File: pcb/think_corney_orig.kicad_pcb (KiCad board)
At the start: 2 copper layers, 128.7 x 86.7 mm, 51 parts

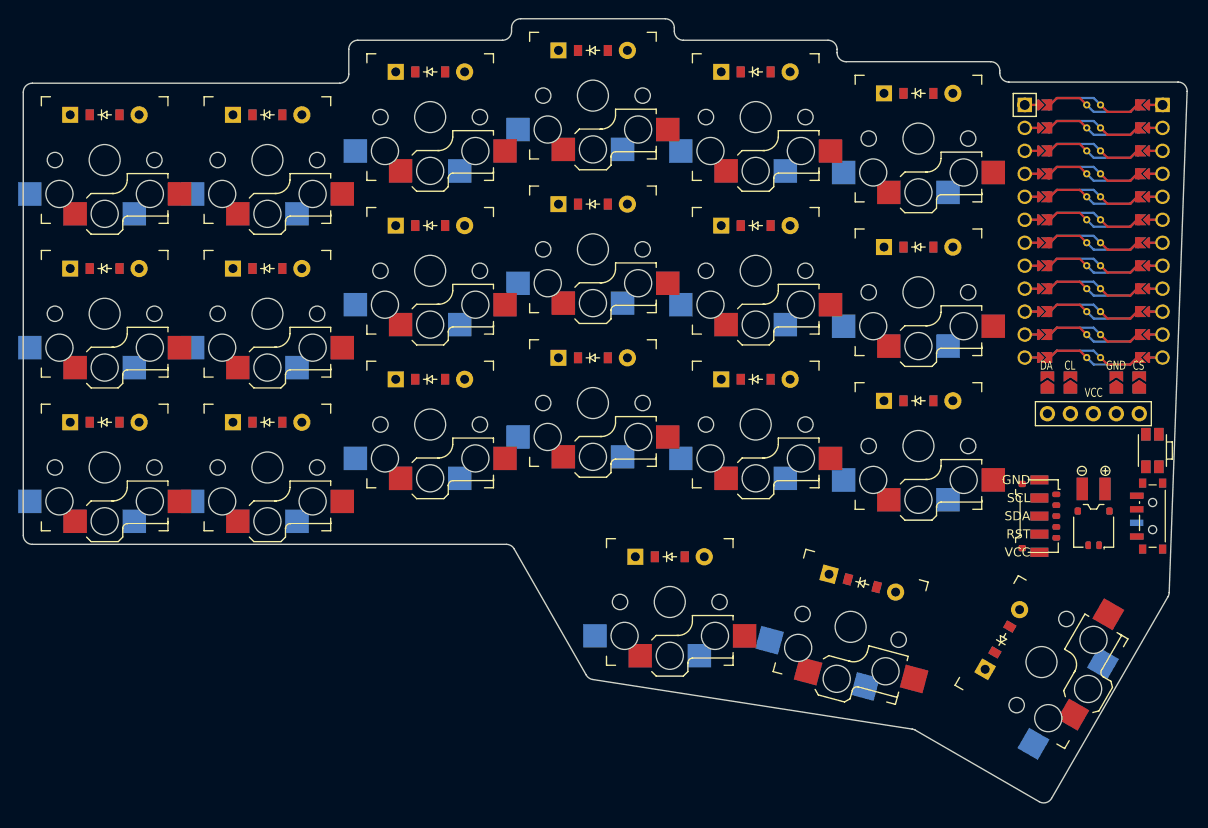
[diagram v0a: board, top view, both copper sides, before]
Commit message: PCB: Add generated pcb version
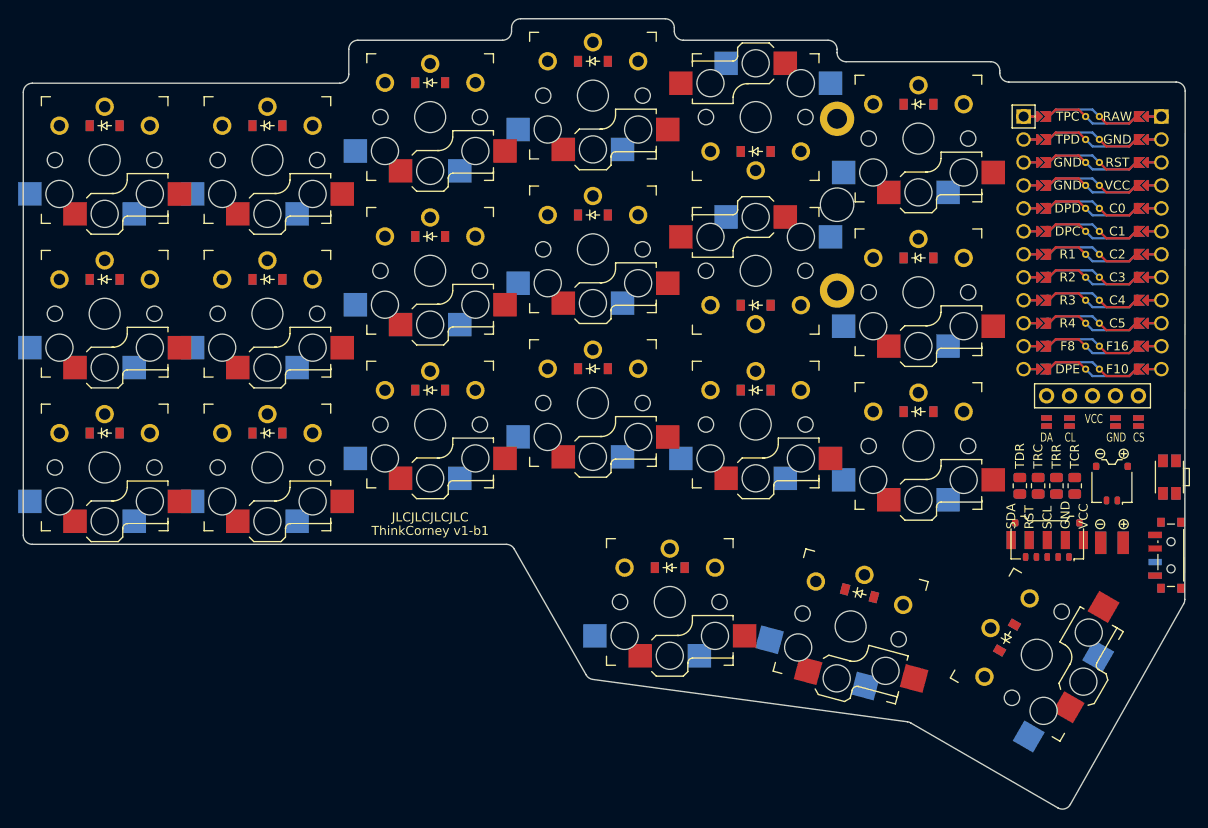
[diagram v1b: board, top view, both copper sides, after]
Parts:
- added ?: , text, F.Cu at (136.0, 107.0)
- added ?: , text, F.Cu at (136.0, 105.5)
- added ICON2: , icon_bat, F.Cu at (211.4, 106.3)
- added SMD1: , smd_805, F.Cu at (204.2, 102.0)
- added TP1: , trackpoint_mount_t430, F.Cu at (181.0, 70.9)
- moved S21 68.1 mm to (172.0, 61.2), turned to 0 degrees
- moved D21 60.5 mm to (172.0, 65.0), turned to 0 degrees
- moved D18 55.7 mm to (183.5, 113.9), turned to -15 degrees
- moved S18 54.5 mm to (182.5, 117.6), turned to -195 degrees
- moved D17 44.9 mm to (162.5, 111.1)
- moved S17 43.9 mm to (162.5, 114.9)
- moved S19 41.0 mm to (203.1, 120.7), turned to -120 degrees
- moved S20 40.8 mm to (172.0, 78.2), turned to 0 degrees
- moved D19 38.4 mm to (199.8, 118.8), turned to 60 degrees
- moved S16 34.0 mm to (190.0, 63.6)
- moved D20 32.9 mm to (172.0, 82.0), turned to 0 degrees
- moved D16 32.8 mm to (190.0, 59.8)
- moved D14 27.3 mm to (190.0, 93.8)
- moved D15 27.3 mm to (190.0, 76.8)
- moved S14 26.4 mm to (190.0, 97.6)
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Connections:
- net P10 renamed F10
- net P16 renamed F16
- net P19 renamed C2
- net P20 renamed C1
- net P21 renamed C0
- net P8 renamed F8
- net TP_RST renamed TPR
- CONN2 pad 1: TP_GND -> VCC
- CONN2 pad 2: TP_SCL -> GND
- CONN2 pad 3: TP_SDA -> TPC
- CONN2 pad 5: TP_VCC -> TPD
- D1 pad 1: P6 -> R3
- D10 pad 1: P6 -> R3
- D11 pad 1: P5 -> R2
- D12 pad 1: P4 -> R1
- D13 pad 1: P6 -> R3
- D14 pad 1: P5 -> R3
- D14 pad 2: index_home -> inner_bottom
- D15 pad 1: P4 -> R2
- D15 pad 2: index_top -> inner_home
- D16 pad 1: P6 -> R1
- D16 pad 2: inner_bottom -> inner_top
- D17 pad 1: P5 -> R4
- D17 pad 2: inner_home -> outer_cluster
- D18 pad 1: P4 -> R4
- D18 pad 2: inner_top -> home_cluster
- D19 pad 1: P7 -> R4
- D19 pad 2: outer_cluster -> inner_cluster
- D2 pad 1: P5 -> R2
- D20 pad 1: P7 -> R2
- D20 pad 2: home_cluster -> index_home
- D21 pad 1: P7 -> R1
- D21 pad 2: inner_cluster -> index_top
- D3 pad 1: P4 -> R1
- D4 pad 1: P6 -> R3
- D5 pad 1: P5 -> R2
- D6 pad 1: P4 -> R1
- D7 pad 1: P6 -> R3
- D8 pad 1: P5 -> R2
- D9 pad 1: P4 -> R1
- DISP1 pad 10: DISP1_1 -> DPD
- DISP1 pad 11: DISP1_2 -> DPC
- DISP1 pad 12: DISP1_4 -> GND
- DISP1 pad 13: DISP1_5 -> DPE
- DISP1 pad 14: P2 -> DISP1_1
- DISP1 pad 15: P3 -> DISP1_2
- DISP1 pad 16: GND -> DISP1_4
- DISP1 pad 17: P9 -> DISP1_5
- DISP1 pad 20: DISP1_5 -> DPD
- DISP1 pad 21: DISP1_4 -> DPC
- DISP1 pad 22: DISP1_2 -> GND
- DISP1 pad 23: DISP1_1 -> DPE
- DISP1 pad 24: P2 -> DISP1_5
- DISP1 pad 25: P3 -> DISP1_4
- DISP1 pad 26: GND -> DISP1_2
- DISP1 pad 27: P9 -> DISP1_1
- DISP1 pad 3: (no net) -> VCC
- PAD2 pad 1: TP_VCC -> TPD
- PAD2 pad 3: TP_SDA -> TPC
- PAD2 pad 4: TP_SCL -> GND
- PAD2 pad 5: TP_GND -> VCC
- S10 pad 1: P18 -> C3
- S11 pad 1: P18 -> C3
- S12 pad 1: P18 -> C3
- S13 pad 1: P15 -> C4
- S14 pad 1: P15 -> C5
- S14 pad 2: index_home -> inner_bottom
- S15 pad 1: P15 -> C5
- S15 pad 2: index_top -> inner_home
- S16 pad 1: P14 -> C5
- S16 pad 2: inner_bottom -> inner_top
- S17 pad 1: P14 -> C3
- S17 pad 2: inner_home -> outer_cluster
- S18 pad 1: P14 -> C4
- S18 pad 2: inner_top -> home_cluster
- S19 pad 1: P18 -> C5
- S19 pad 2: outer_cluster -> inner_cluster
- S20 pad 1: P15 -> C4
- S20 pad 2: home_cluster -> index_home
- S21 pad 1: P14 -> C4
- S21 pad 2: inner_cluster -> index_top
- _1 pad 10: P14 -> C5
- _1 pad 13: P9 -> DPE
- _1 pad 15: P7 -> R4
- _1 pad 16: P6 -> R3
- _1 pad 17: P5 -> R2
- _1 pad 18: P4 -> R1
- _1 pad 19: P3 -> DPC
- _1 pad 20: P2 -> DPD
- _1 pad 23: P0 -> TPD
- _1 pad 24: P1 -> TPC
- _1 pad 8: P18 -> C3
- _1 pad 9: P15 -> C4
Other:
- board size 128.7 x 86.7 mm -> 128.5 x 87.4 mm

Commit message: KiCad: Fix many DRC problems
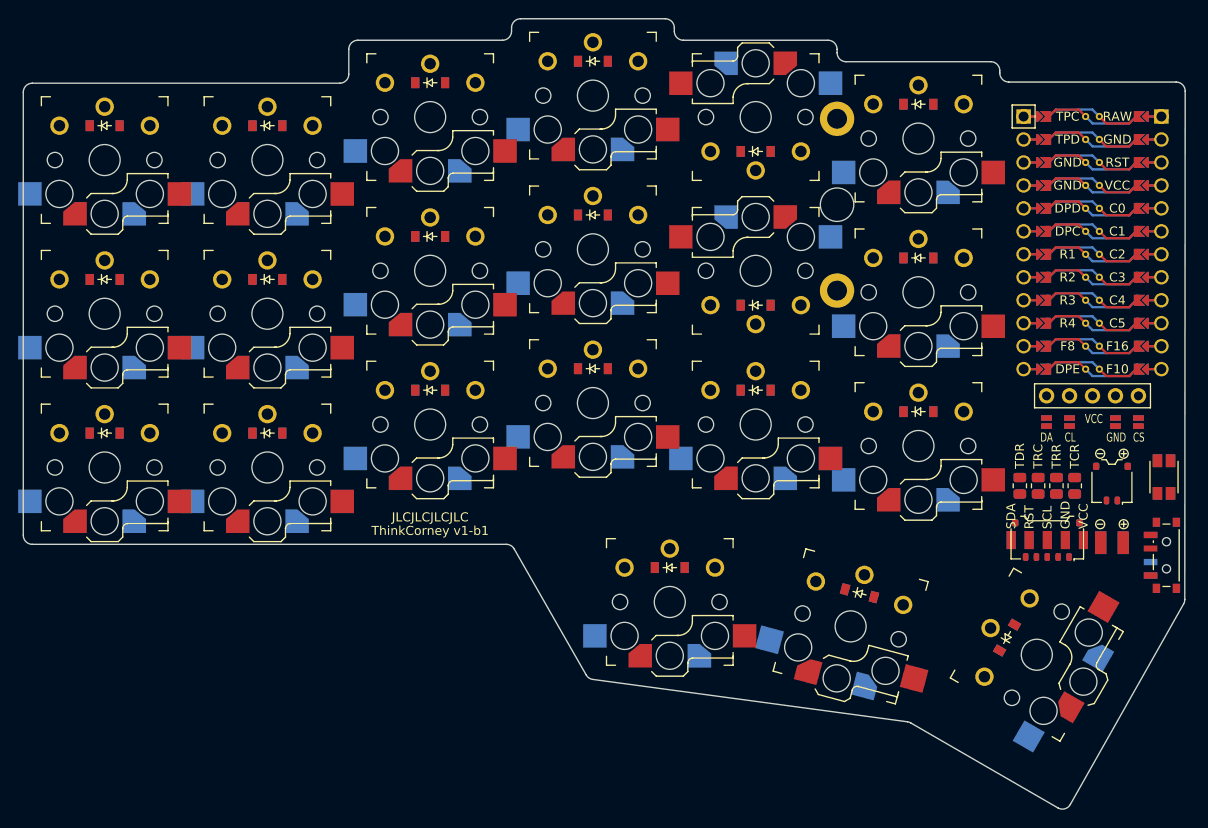
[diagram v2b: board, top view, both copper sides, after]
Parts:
- removed CONN3: , sw_reset_side
- added SW2: , sw_reset_side, F.Cu at (217.2, 101.1)
- moved SW1 0.50 mm to (217.4, 109.7)
